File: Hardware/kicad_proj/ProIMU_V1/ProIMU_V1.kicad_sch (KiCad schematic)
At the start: 35 parts, among them J1 Conn_01x04, J4 502570-0893, U1 ADM101E, U2 TJA1051T-3, U4 AIR602, U5 BMP280, U6 MPU-9250

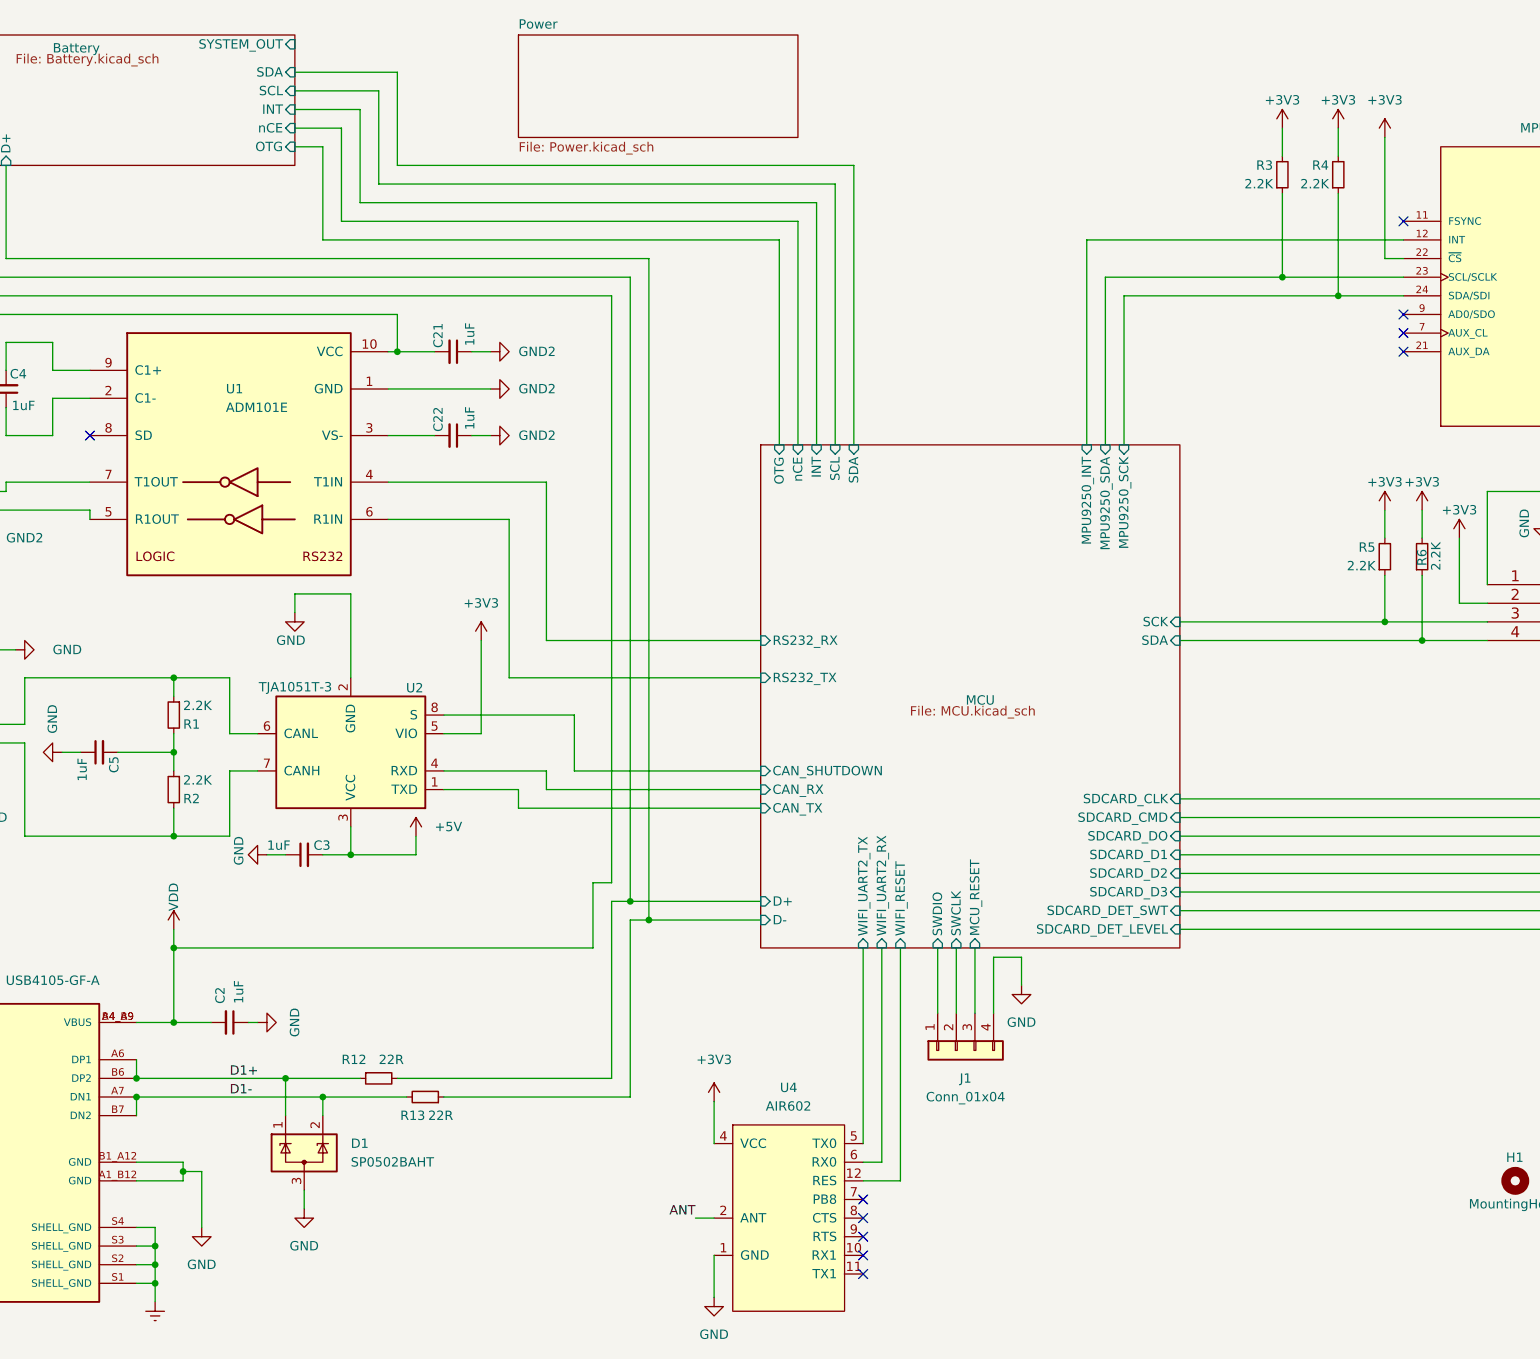
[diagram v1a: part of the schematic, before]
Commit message: Updated schematic, layout and footprints
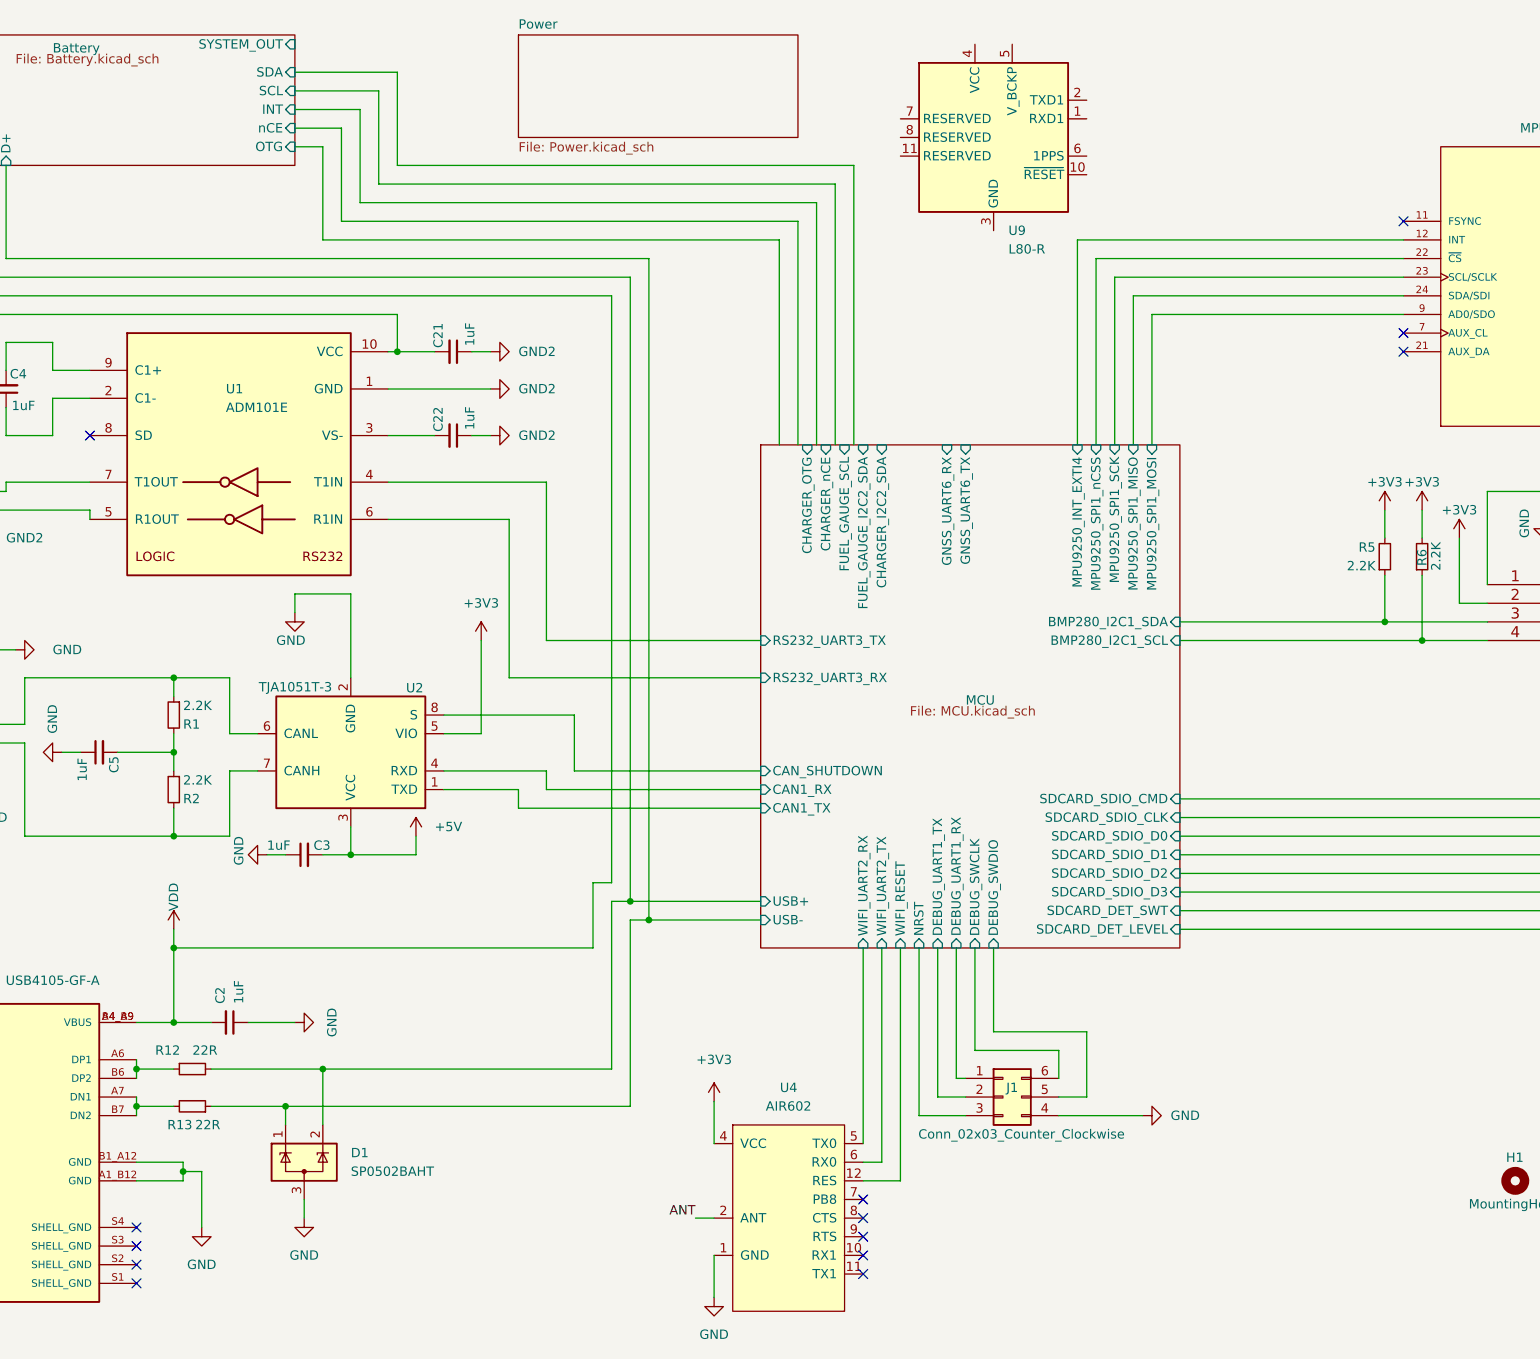
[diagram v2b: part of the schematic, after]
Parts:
- removed J1: Conn_01x04, Connector_PinHeader_2.54mm:PinHeader_2x02_P2.54mm_Vertical_SMD, symbol Connector_Generic:Conn_01x04
- removed R3, R4: 2.2K, Resistor_SMD:R_0402_1005Metric_Pad0.72x0.64mm_HandSolder, symbol Device:R_Small
- added J1: Conn_02x03_Counter_Clockwise, Connector_PinHeader_2.54mm:PinHeader_2x03_P2.54mm_Vertical_SMD, symbol Connector_Generic:Conn_02x03_Counter_Clockwise
- added U9: L80-R, RF_GPS:Quectel_L80-R, symbol RF_GPS:L80-R
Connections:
- net +3V3: no longer U6.22 (~{CS})
- net Battery/D+: now also D1.1 (K)
- net Battery/D-: now also D1.2 (K)
- net GND: now also J1.4 (Pin_4)
- net MCU/WIFI_UART2_RX: now also U4.5 (TX0); no longer U4.6 (RX0)
- net MCU/WIFI_UART2_TX: now also U4.6 (RX0); no longer U4.5 (TX0)
- net MCU/MPU9250_SPI1_MOSI: now reaches U6.9 (AD0/SDO)
- net D1+: no longer names the net of R12.1, USB1.A6 (DP1), USB1.B6 (DP2)
- net D1+: no longer D1.1 (K)
- net D1-: no longer names the net of R13.2, USB1.A7 (DN1), USB1.B7 (DN2)
- net D1-: no longer D1.2 (K)
- removed net Earth: USB1.S1 (SHELL_GND), USB1.S2 (SHELL_GND), USB1.S3 (SHELL_GND), USB1.S4 (SHELL_GND)
- net MCU/CAN_RX renamed MCU/CAN1_RX
- net MCU/CAN_TX renamed MCU/CAN1_TX
- net MCU/MPU9250_INT renamed MCU/MPU9250_INT_EXTI4
- net MCU/MPU9250_SCK renamed MCU/MPU9250_SPI1_MISO
- net MCU/MPU9250_SDA renamed MCU/MPU9250_SPI1_SCK
- net MCU/RS232_RX renamed MCU/RS232_UART3_TX
- net MCU/RS232_TX renamed MCU/RS232_UART3_RX
- net MCU/SCK renamed MCU/BMP280_I2C1_SDA
- net MCU/SDA renamed MCU/BMP280_I2C1_SCL
- net MCU/SDCARD_CLK renamed MCU/SDCARD_SDIO_CMD
- net MCU/SDCARD_CMD renamed MCU/SDCARD_SDIO_CLK
- net MCU/SDCARD_D1 renamed MCU/SDCARD_SDIO_D1
- net MCU/SDCARD_D2 renamed MCU/SDCARD_SDIO_D2
- net MCU/SDCARD_D3 renamed MCU/SDCARD_SDIO_D3
- net MCU/SDCARD_DO renamed MCU/SDCARD_SDIO_D0
- new net: U9.12 (GND), U9.3 (GND)
- new net MCU/DEBUG_SWCLK: J1.6 (Pin_6)
- new net MCU/DEBUG_SWDIO: J1.5 (Pin_5)
- new net MCU/DEBUG_UART1_RX: J1.1 (Pin_1)
- new net MCU/DEBUG_UART1_TX: J1.2 (Pin_2)
- new net MCU/MPU9250_SPI1_nCSS: U6.22 (~{CS})
- new net MCU/NRST: J1.3 (Pin_3)
- no-connect marks 15 -> 18
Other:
- sheet MCU ports: added BMP280_I2C1_SCL, BMP280_I2C1_SDA, CAN1_RX, CAN1_TX, CHARGER_I2C2_SDA, CHARGER_OTG, CHARGER_nCE, DEBUG_SWCLK, DEBUG_SWDIO, DEBUG_UART1_RX, DEBUG_UART1_TX, FUEL_GAUGE_I2C2_SDA, FUEL_GAUGE_SCL, GNSS_UART6_RX, GNSS_UART6_TX, MPU9250_INT_EXTI4, MPU9250_SPI1_MISO, MPU9250_SPI1_MOSI, MPU9250_SPI1_SCK, MPU9250_SPI1_nCSS, NRST, RS232_UART3_RX, RS232_UART3_TX, SDCARD_SDIO_CLK, SDCARD_SDIO_CMD, SDCARD_SDIO_D0, SDCARD_SDIO_D1, SDCARD_SDIO_D2, SDCARD_SDIO_D3, USB+, USB-; removed CAN_RX, CAN_TX, D+, D-, INT, MCU_RESET, MPU9250_INT, MPU9250_SCK, MPU9250_SDA, OTG, RS232_RX, RS232_TX, SCK, SCL, SDA, SDCARD_CLK, SDCARD_CMD, SDCARD_D1, SDCARD_D2, SDCARD_D3, SDCARD_DO, SWCLK, SWDIO, nCE
- moved on the sheet: D1, R12, R13

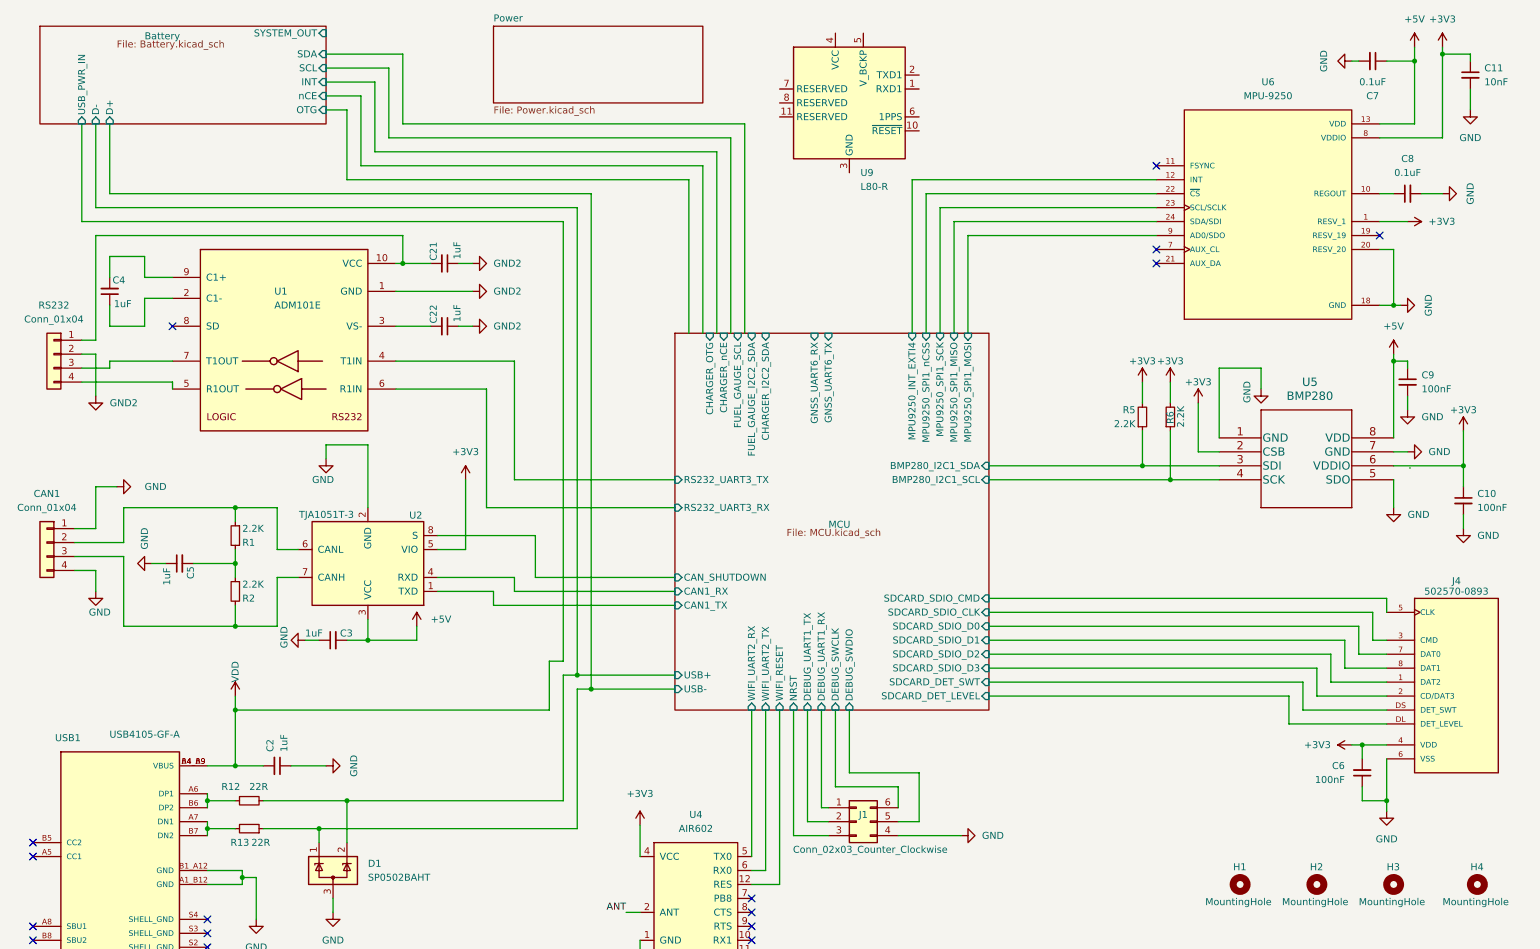
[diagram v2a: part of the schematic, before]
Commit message: Updated Layout, schematic, added new symbol and footprint
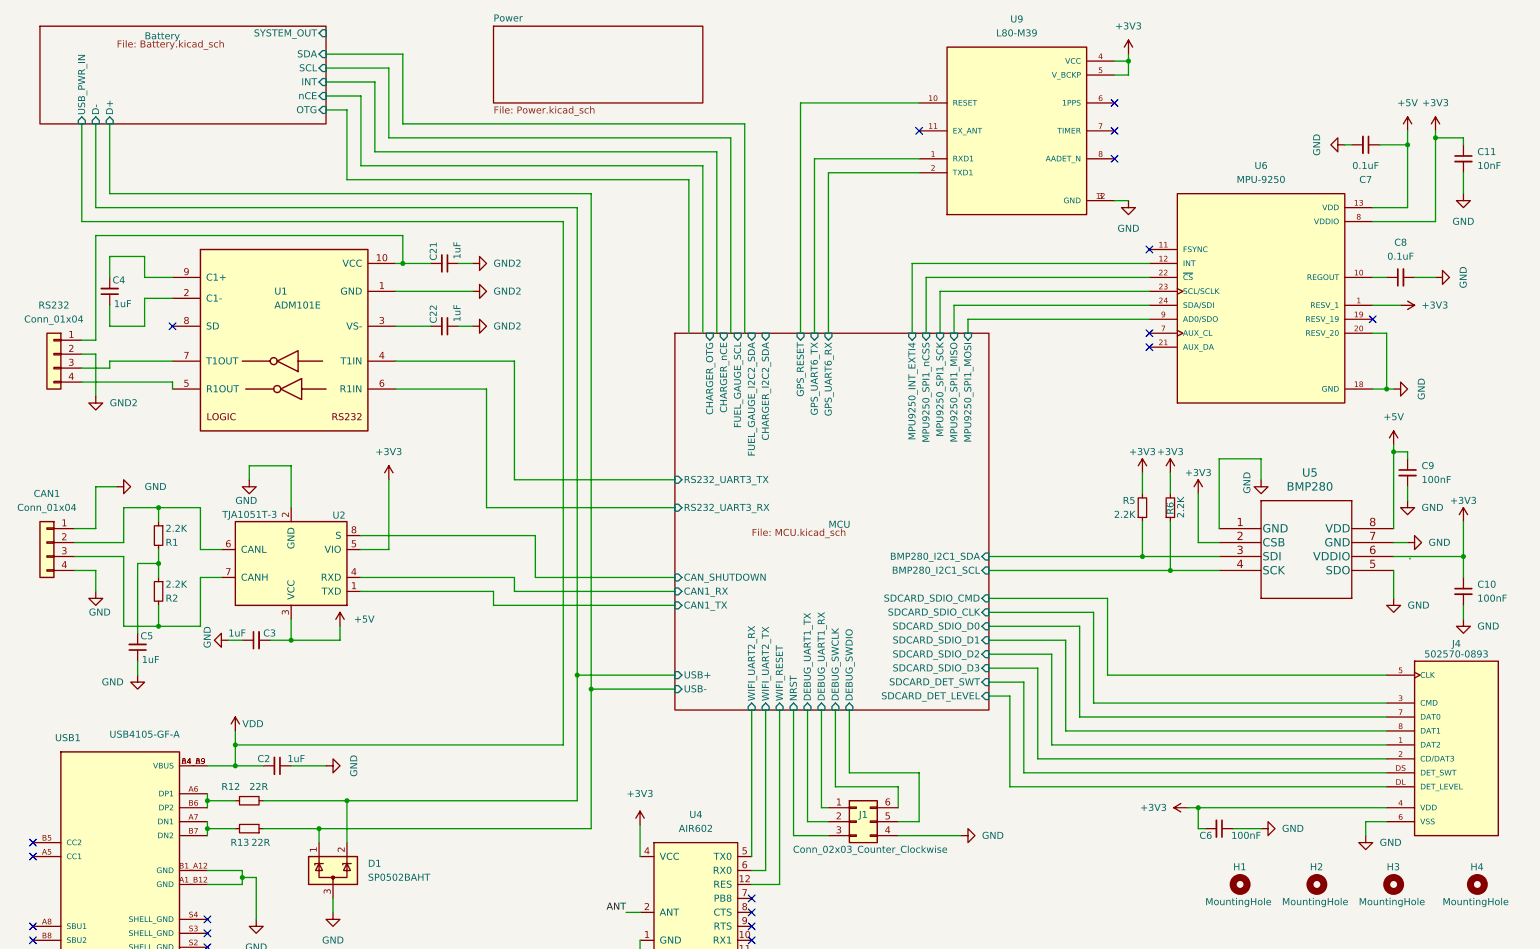
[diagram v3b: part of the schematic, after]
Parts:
- removed U9: L80-R, RF_GPS:Quectel_L80-R, symbol RF_GPS:L80-R
- added U9: L80-M39, footprints:XCVR_L80-M39, symbol L80-M39:L80-M39
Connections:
- net +3V3: now also U9.4 (VCC), U9.5 (V_BCKP)
- net GND: now also U9.12 (GND), U9.3 (GND)
- new net MCU/GPS_RESET: U9.10 (RESET)
- new net MCU/GPS_UART6_RX: U9.2 (TXD1)
- new net MCU/GPS_UART6_TX: U9.1 (RXD1)
- no-connect marks 18 -> 22
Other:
- sheet MCU ports: added GPS_RESET, GPS_UART6_RX, GPS_UART6_TX; removed GNSS_UART6_RX, GNSS_UART6_TX
- moved on the sheet: C10, C11, C3, C5, C6, C7, C8, C9, J4, R1, R2, R5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

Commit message: Updated Schematic and Layout
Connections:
- net GND: no longer C5.1, CAN1.1 (Pin_1), CAN1.4 (Pin_4)
- new net: C5.1, CAN1.1 (Pin_1), CAN1.4 (Pin_4)
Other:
- moved on the sheet: C10, C11, C2, C21, C22, C3, C4, C5, C6, C7, C8, C9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

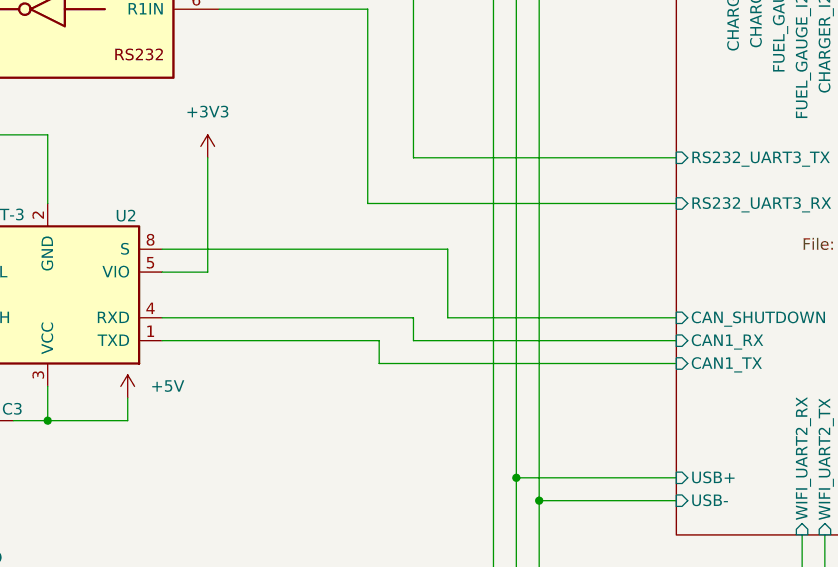
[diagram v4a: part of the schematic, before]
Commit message: Updated layout
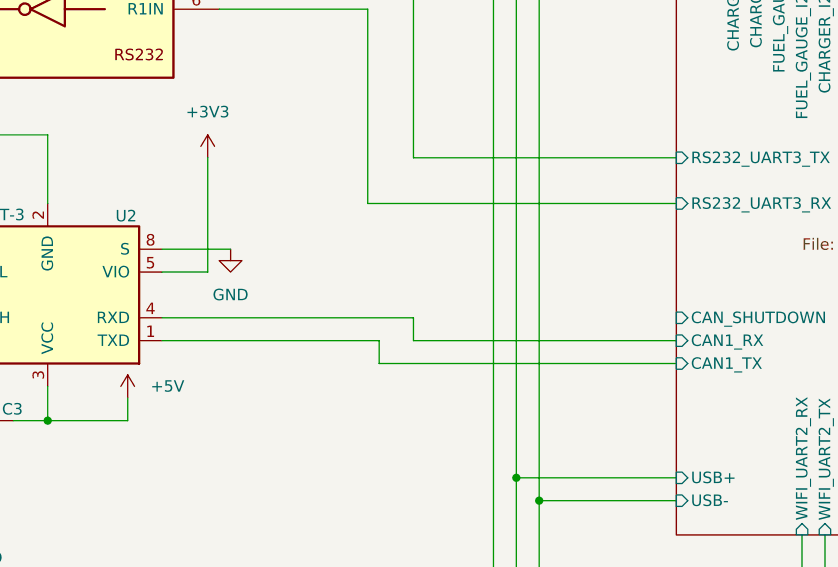
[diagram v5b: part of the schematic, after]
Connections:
- net GND: now also U2.8 (S)
- net MCU/CAN_SHUTDOWN: no longer U2.8 (S)
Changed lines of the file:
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@@
-    (stroke (width 0) (type default) (color 0 0 0 0))
-  )
-  (wire (pts (xy 394.97 113.03) (xy 394.97 120.65))
     (stroke (width 0) (type default) (color 0 0 0 0))
   )
@@
     (stroke (width 0) (type default) (color 0 0 0 0))
   )
+  (wire (pts (xy 363.22 113.03) (xy 370.84 113.03))
+    (stroke (width 0) (type default) (color 0 0 0 0))
+  )
   (wire (pts (xy 405.13 50.8) (xy 405.13 140.97))
     (stroke (width 0) (type default) (color 0 0 0 0))
@@
     (stroke (width 0) (type default) (color 0 0 0 0))
   )
-  (wire (pts (xy 363.22 113.03) (xy 394.97 113.03))
-    (stroke (width 0) (type default) (color 0 0 0 0))
-  )
   (wire (pts (xy 368.3 115.57) (xy 368.3 102.87))
     (stroke (width 0) (type default) (color 0 0 0 0))
@@
   )
   (wire (pts (xy 434.34 173.99) (xy 436.88 173.99))
-    (stroke (width 0) (type default) (color 0 0 0 0))
-  )
-  (wire (pts (xy 394.97 120.65) (xy 420.37 120.65))
     (stroke (width 0) (type default) (color 0 0 0 0))
   )
@@
     )
     (property "Datasheet" "" (id 3) (at 527.05 166.37 0)
+      (effects (font (size 1.27 1.27)) hide)
+    )
+    (pin "1")
+  )
+  (symbol (lib_id "power:GND") (at 370.84 113.03 0) (unit 1)
+    (in_bom yes) (on_board yes) (fields_autoplaced)
+    (property "Reference" "#PWR?" (id 0) (at 370.84 119.38 0)
+      (effects (font (size 1.27 1.27)) hide)
+    )
+    (property "Value" "GND" (id 1) (at 370.84 118.11 0))
+    (property "Footprint" "" (id 2) (at 370.84 113.03 0)
+      (effects (font (size 1.27 1.27)) hide)
+    )
+    (property "Datasheet" "" (id 3) (at 370.84 113.03 0)
       (effects (font (size 1.27 1.27)) hide)
     )
@@
       (reference "#PWR0114") (unit 1) (value "GND") (footprint "")
     )
+    (path "/0c260b7f-009c-452c-a58b-377080500162"
+      (reference "#PWR?") (unit 1) (value "GND") (footprint "")
+    )
     (path "/09535cde-9ba2-41fd-bb26-86cd9c93b7a7/e67f3a4a-b4bb-4b38-a7f4-b0011cb79e12"
